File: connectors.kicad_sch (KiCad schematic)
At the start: 9 parts

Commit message: Split PC_DETECT and POWER_OFF lines
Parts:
- removed R?: 100k, Resistor_SMD:R_0402_1005Metric, symbol Device:R
- added R?: 100k, Resistor_SMD:R_0402_1005Metric, symbol Device:R
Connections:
- net +3V3: now also R?.1
- net GND: no longer P?.3 (GND)
- net PC_DET/POWER_OFF renamed POWER_OFF
- new net PC_DETECT: P?.3 (GND), R?.2
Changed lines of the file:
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@@
   (junction (at 153.67 126.365) (diameter 0) (color 0 0 0 0)
   )
-  (junction (at 153.67 136.525) (diameter 0) (color 0 0 0 0)
-  )
   (junction (at 153.67 103.505) (diameter 0) (color 0 0 0 0)
   )
   (junction (at 153.67 118.745) (diameter 0) (color 0 0 0 0)
   )
+  (junction (at 172.085 151.13) (diameter 0) (color 0 0 0 0)
+  )
   (junction (at 222.885 50.8) (diameter 0) (color 0 0 0 0)
   )
@@
   )
   (junction (at 83.82 53.975) (diameter 0) (color 0 0 0 0)
-  )
-  (junction (at 67.31 156.21) (diameter 0) (color 0 0 0 0)
   )
   (junction (at 153.67 80.645) (diameter 0) (color 0 0 0 0)
@@
     (stroke (width 0) (type default) (color 0 0 0 0))
   )
-  (wire (pts (xy 153.67 136.525) (xy 153.67 142.875))
-    (stroke (width 0) (type default) (color 0 0 0 0))
-  )
   (wire (pts (xy 225.425 95.885) (xy 220.345 95.885))
     (stroke (width 0) (type default) (color 0 0 0 0))
@@
     (stroke (width 0) (type default) (color 0 0 0 0))
   )
+  (wire (pts (xy 151.13 136.525) (xy 160.02 136.525))
+    (stroke (width 0) (type default) (color 0 0 0 0))
+  )
   (wire (pts (xy 83.82 53.975) (xy 83.82 51.435))
     (stroke (width 0) (type default) (color 0 0 0 0))
@@
     (stroke (width 0) (type default) (color 0 0 0 0))
   )
-  (bus (pts (xy 45.72 123.825) (xy 74.295 123.825))
+  (wire (pts (xy 160.02 151.13) (xy 172.085 151.13))
     (stroke (width 0) (type default) (color 0 0 0 0))
   )
@@
     (stroke (width 0) (type default) (color 0 0 0 0))
   )
+  (wire (pts (xy 172.085 149.86) (xy 172.085 151.13))
+    (stroke (width 0) (type default) (color 0 0 0 0))
+  )
   (wire (pts (xy 220.345 103.505) (xy 225.425 103.505))
     (stroke (width 0) (type default) (color 0 0 0 0))
@@
     (stroke (width 0) (type default) (color 0 0 0 0))
   )
-  (wire (pts (xy 67.31 156.21) (xy 76.2 156.21))
-    (stroke (width 0) (type default) (color 0 0 0 0))
-  )
   (polyline (pts (xy 231.775 65.405) (xy 231.775 78.74))
     (stroke (width 0) (type default) (color 0 0 0 0))
@@
     (stroke (width 0) (type default) (color 0 0 0 0))
   )
-  (wire (pts (xy 151.13 136.525) (xy 153.67 136.525))
-    (stroke (width 0) (type default) (color 0 0 0 0))
-  )
   (bus (pts (xy 69.85 89.535) (xy 69.85 92.075))
     (stroke (width 0) (type default) (color 0 0 0 0))
@@
     (stroke (width 0) (type default) (color 0 0 0 0))
   )
+  (wire (pts (xy 160.02 136.525) (xy 160.02 151.13))
+    (stroke (width 0) (type default) (color 0 0 0 0))
+  )
   (wire (pts (xy 53.975 139.065) (xy 53.975 140.335))
     (stroke (width 0) (type default) (color 0 0 0 0))
@@
     (stroke (width 0) (type default) (color 0 0 0 0))
   )
-  (wire (pts (xy 62.23 156.21) (xy 67.31 156.21))
+  (wire (pts (xy 62.23 156.21) (xy 76.2 156.21))
     (stroke (width 0) (type default) (color 0 0 0 0))
   )
@@
     (stroke (width 0) (type default) (color 0 0 0 0))
   )
+  (bus (pts (xy 46.355 123.825) (xy 74.295 123.825))
+    (stroke (width 0) (type default) (color 0 0 0 0))
+  )
   (wire (pts (xy 153.67 80.645) (xy 153.67 88.265))
     (stroke (width 0) (type default) (color 0 0 0 0))
@@
     (stroke (width 0) (type default) (color 0 0 0 0))
   )
-  (wire (pts (xy 153.67 133.985) (xy 153.67 136.525))
+  (wire (pts (xy 153.67 133.985) (xy 153.67 142.875))
     (stroke (width 0) (type default) (color 0 0 0 0))
   )
@@
     (stroke (width 0) (type default) (color 0 0 0 0))
   )
+  (wire (pts (xy 177.165 151.13) (xy 172.085 151.13))
+    (stroke (width 0) (type default) (color 0 0 0 0))
+  )
   (bus (pts (xy 172.085 67.945) (xy 172.085 70.485))
     (stroke (width 0) (type default) (color 0 0 0 0))
@@
   )
   (wire (pts (xy 73.66 130.175) (xy 73.66 153.67))
-    (stroke (width 0) (type default) (color 0 0 0 0))
-  )
-  (wire (pts (xy 67.31 156.21) (xy 67.31 157.48))
     (stroke (width 0) (type default) (color 0 0 0 0))
   )
@@
     (effects (font (size 1.27 1.27)) (justify right bottom))
   )
-  (label "I^{2}S.FS" (at 84.455 112.395 180)
+  (label "I^{2}S.FS" (at 83.82 112.395 180)
     (effects (font (size 1.27 1.27)) (justify right bottom))
   )
@@
     (effects (font (size 1.27 1.27)) (justify right bottom))
   )
-  (label "I^{2}S.MCK" (at 84.455 120.015 180)
-    (effects (font (size 1.27 1.27)) (justify right bottom))
+  (label "I^{2}S.MCK" (at 78.105 120.015 0)
+    (effects (font (size 1.27 1.27)) (justify left bottom))
   )
   (label "UART.RX" (at 77.47 86.995 0)
@@
     (effects (font (size 1.27 1.27)) (justify left bottom))
   )
-  (label "I^{2}S.SDO" (at 84.455 114.935 180)
-    (effects (font (size 1.27 1.27)) (justify right bottom))
+  (label "I^{2}S.SDO" (at 78.105 114.935 0)
+    (effects (font (size 1.27 1.27)) (justify left bottom))
   )
   (label "USB.D-" (at 167.005 128.905 180)
@@
     (effects (font (size 1.27 1.27)) (justify left bottom))
   )
-  (label "I^{2}S.SDI" (at 84.455 109.855 180)
-    (effects (font (size 1.27 1.27)) (justify right bottom))
+  (label "I^{2}S.SDI" (at 78.105 109.855 0)
+    (effects (font (size 1.27 1.27)) (justify left bottom))
   )
   (label "SPI.SDI" (at 163.195 65.405 180)
@@
     (effects (font (size 1.27 1.27)) (justify left bottom))
   )
-  (label "I^{2}S.SCK" (at 84.455 117.475 180)
-    (effects (font (size 1.27 1.27)) (justify right bottom))
+  (label "I^{2}S.SCK" (at 78.105 117.475 0)
+    (effects (font (size 1.27 1.27)) (justify left bottom))
   )
   (label "I^{2}C.SDA" (at 84.455 92.075 180)
@@
     (effects (font (size 1.27 1.27)) (justify left bottom))
   )
-  (hierarchical_label "PC_DET{slash}POWER_OFF" (shape output) (at 62.23 156.21 180)
+  (hierarchical_label "POWER_OFF" (shape output) (at 62.23 156.21 180)
     (effects (font (size 1.27 1.27)) (justify right))
   )
@@
     (effects (font (size 1.27 1.27)) (justify right))
   )
+  (hierarchical_label "PC_DETECT" (shape output) (at 177.165 151.13 0)
+    (effects (font (size 1.27 1.27)) (justify left))
+  )
   (hierarchical_label "SWD" (shape passive) (at 272.415 107.315 0)
     (effects (font (size 1.27 1.27)) (justify left))
@@
   (hierarchical_label "PA_EN" (shape input) (at 87.63 64.135 180)
     (effects (font (size 1.27 1.27)) (justify right))
-  )
-  (symbol (lib_id "power:GND") (at 67.31 165.1 0) (unit 1)
-    (in_bom yes) (on_board yes)
-    (property "Reference" "#PWR?" (id 0) (at 67.31 171.45 0)
-      (effects (font (size 1.27 1.27)) hide)
-    )
-    (property "Value" "GND" (id 1) (at 67.437 169.4942 0))
-    (property "Footprint" "" (id 2) (at 67.31 165.1 0)
-      (effects (font (size 1.27 1.27)) hide)
-    )
-    (property "Datasheet" "" (id 3) (at 67.31 165.1 0)
-      (effects (font (size 1.27 1.27)) hide)
-    )
-    (pin "1")
   )
   (symbol (lib_id "Transistor_FET:BSS138") (at 51.435 133.985 0) (unit 1)
@@
     )
     (pin "1")
+  )
+  (symbol (lib_id "Device:R") (at 172.085 146.05 0) (mirror y) (unit 1)
+    (in_bom yes) (on_board yes)
+    (property "Reference" "R?" (id 0) (at 175.895 144.78 0)
+      (effects (font (size 1.27 1.27)) (justify left))
+    )
+    (property "Value" "100k" (id 1) (at 178.435 147.32 0)
+      (effects (font (size 1.27 1.27)) (justify left))
+    )
+    (property "Footprint" "Resistor_SMD:R_0402_1005Metric" (id 2) (at 173.863 146.05 90)
+      (effects (font (size 1.27 1.27)) hide)
+    )
+    (property "Datasheet" "~" (id 3) (at 172.085 146.05 0)
+      (effects (font (size 1.27 1.27)) hide)
+    )
+    (pin "1")
+    (pin "2")
   )
   (symbol (lib_id "Connector_Generic:Conn_02x04_Counter_Clockwise") (at 230.505 98.425 0) (unit 1)
@@
     (pin "8")
   )
-  (symbol (lib_id "Device:R") (at 67.31 161.29 0) (unit 1)
-    (in_bom yes) (on_board yes)
-    (property "Reference" "R?" (id 0) (at 63.5 160.02 0)
-      (effects (font (size 1.27 1.27)) (justify left))
-    )
-    (property "Value" "100k" (id 1) (at 60.96 162.56 0)
-      (effects (font (size 1.27 1.27)) (justify left))
-    )
-    (property "Footprint" "Resistor_SMD:R_0402_1005Metric" (id 2) (at 65.532 161.29 90)
-      (effects (font (size 1.27 1.27)) hide)
-    )
-    (property "Datasheet" "~" (id 3) (at 67.31 161.29 0)
-      (effects (font (size 1.27 1.27)) hide)
-    )
-    (pin "1")
-    (pin "2")
-  )
   (symbol (lib_id "power:+3V3") (at 212.725 50.165 0) (unit 1)
     (in_bom yes) (on_board yes)
@@
       (effects (font (size 1.27 1.27)) hide)
     )
+    (pin "1")
+  )
+  (symbol (lib_id "power:+3V3") (at 172.085 142.24 0) (mirror y) (unit 1)
+    (in_bom yes) (on_board yes)
+    (property "Reference" "#PWR?" (id 0) (at 172.085 146.05 0)
+      (effects (font (size 1.27 1.27)) hide)
+    )
+    (property "Value" "+3V3" (id 1) (at 172.72 138.43 0))
+    (property "Footprint" "" (id 2) (at 172.085 142.24 0)
+      (effects (font (size 1.27 1.27)) hide)
+    )
+    (property "Datasheet" "" (id 3) (at 172.085 142.24 0)
+      (effects (font (size 1.27 1.27)) hide)
+    )

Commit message: Connected ADF7021 chip enable to MCU, grouped PTT/W_DISABLE signal with SWDIO
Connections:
- no-connect marks 29 -> 28
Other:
- note added: "Connect to SWDIO line. This is safe to do as SWDIO requires/tolerates an external pullup."
- moved on the sheet: Q?, R?

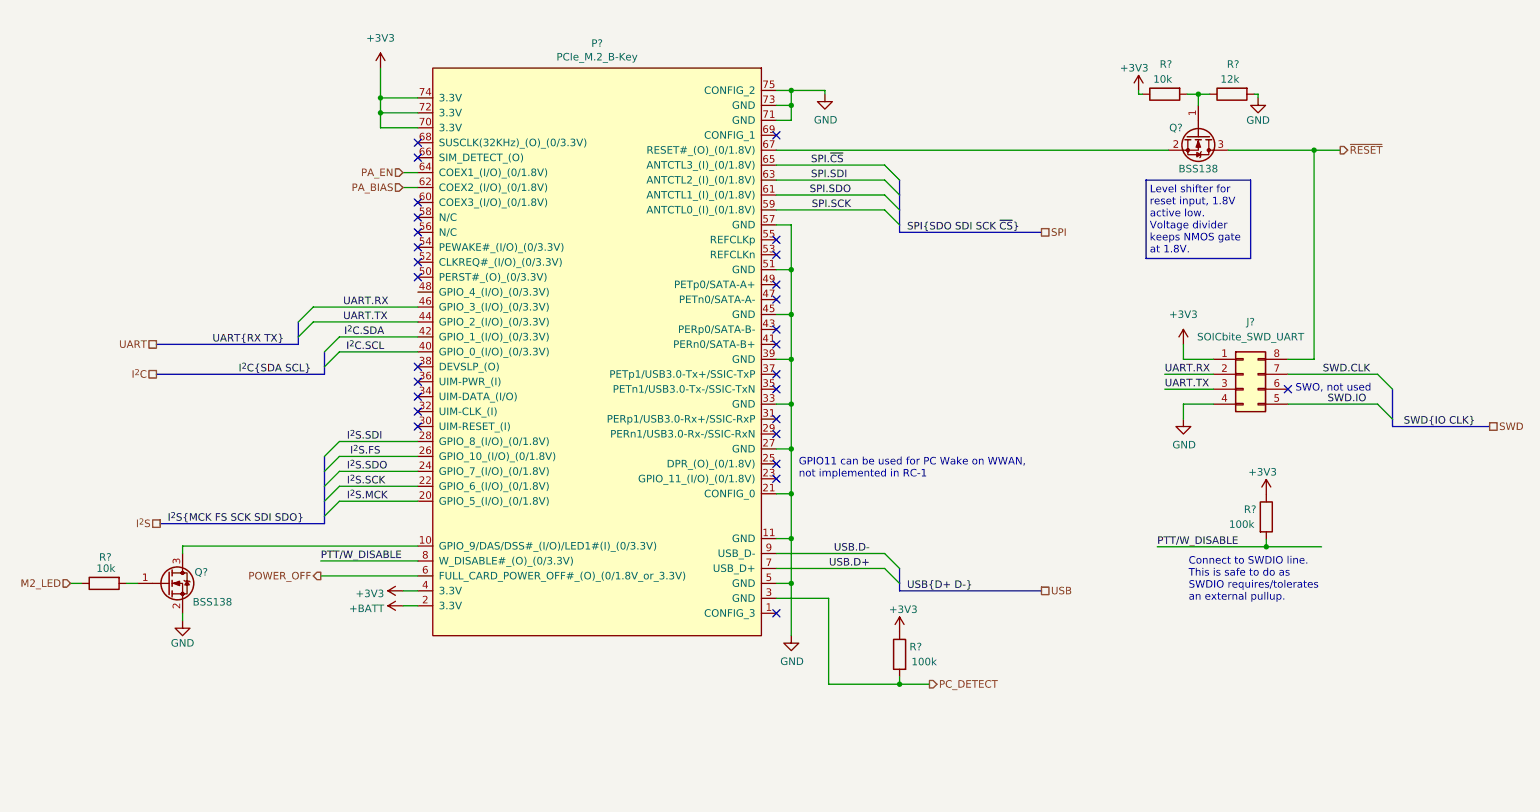
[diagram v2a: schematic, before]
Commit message: Added I2C for external EEPROM on the M.2 connector, added pull-up resistors on the I2C lines
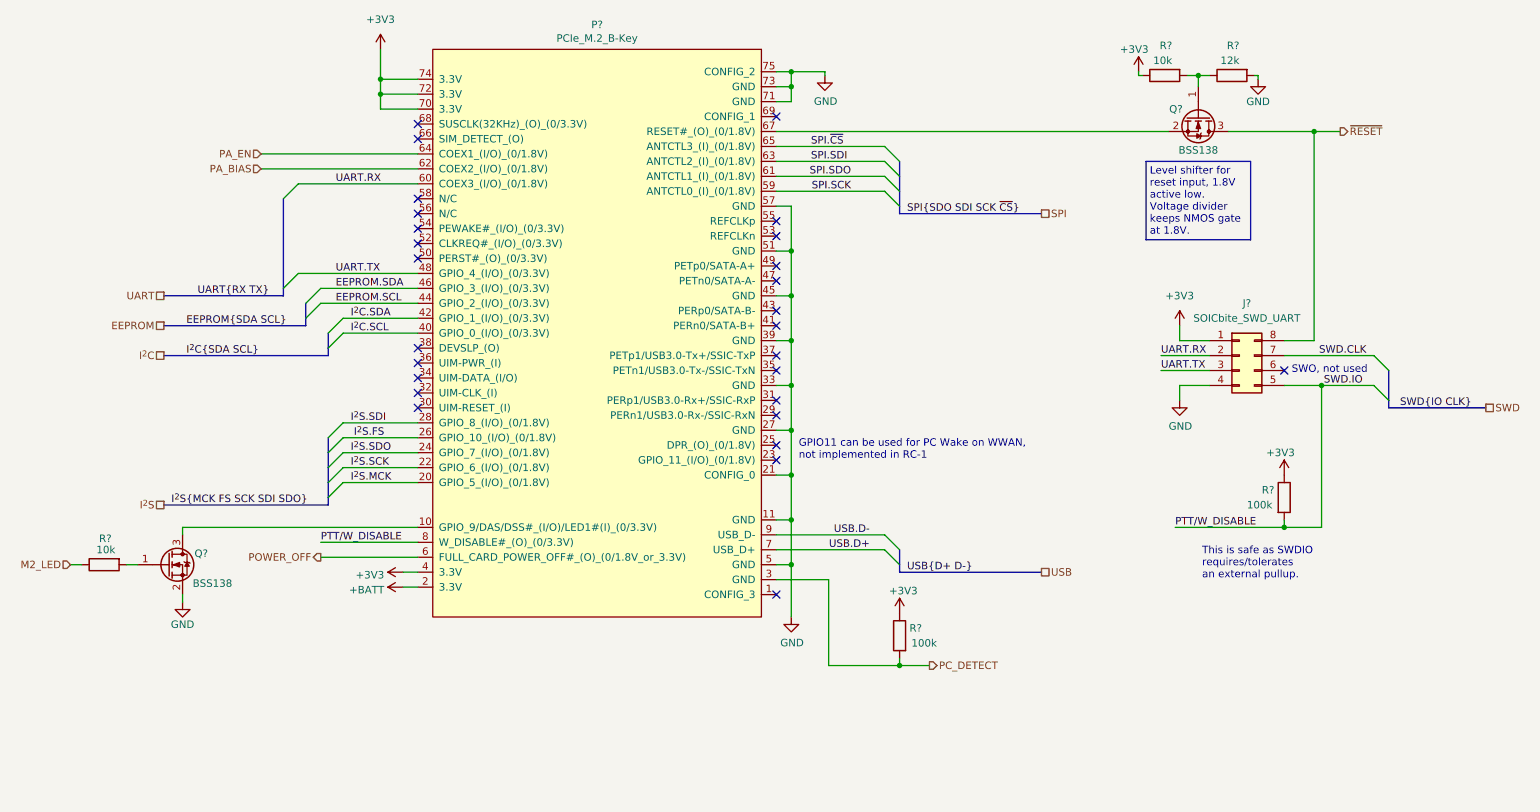
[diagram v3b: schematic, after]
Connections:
- net SWD.IO is gone; now on net PTT/W_DISABLE: J?.5 (Pin_5)
- net UART.RX: now also P?.60 (COEX3_(I/O)_(0/1.8V)); no longer P?.46 (GPIO_3_(I/O)_(0/3.3V))
- net UART.TX: now also P?.48 (GPIO_4_(I/O)_(0/3.3V)); no longer P?.44 (GPIO_2_(I/O)_(0/3.3V))
- new net EEPROM.SCL: P?.44 (GPIO_2_(I/O)_(0/3.3V))
- new net EEPROM.SDA: P?.46 (GPIO_3_(I/O)_(0/3.3V))
- no-connect marks 28 -> 27
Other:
- note added: "This is safe as SWDIO requires/tolerates an external pullup."
- note removed: "Connect to SWDIO line. This is safe to do as SWDIO requires/tolerates an external pullup."
- moved on the sheet: J?, P?, Q?, R?

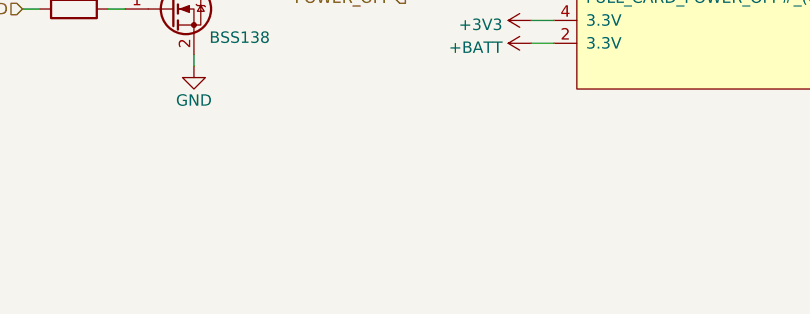
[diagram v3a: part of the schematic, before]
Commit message: Set up ADF7021 for single RF output, 2-point modulation
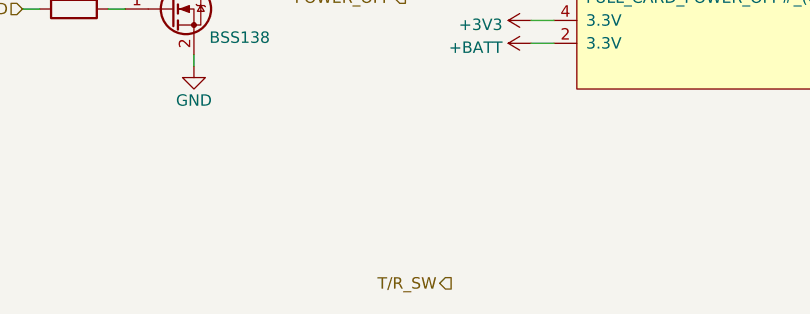
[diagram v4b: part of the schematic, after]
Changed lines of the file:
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@@
+    (effects (font (size 1.27 1.27)) (justify right))
+  )
+  (hierarchical_label "T{slash}R_SW" (shape output) (at 78.74 161.29 180)
     (effects (font (size 1.27 1.27)) (justify right))
   )
